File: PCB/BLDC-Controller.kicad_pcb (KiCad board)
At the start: 2 copper layers, 114.3 x 76.5 mm, 95 parts, among them J1 Prog, J2 Receiver, J3 Bat_In, J4 Mot_Con, J5 Mot_Con, J6 Mot_Con, Q1 P75NF75, Q2 P75NF75, Q3 P75NF75, Q4 P75NF75, Q5 P75NF75, Q6 P75NF75, SW1 RST, SW2 Speed+, SW3 Speed-, U1 UCC27282, U2 UCC27282, U3 UCC27282, U4 ATmega328P-P, U5 LM317, U6 LM7805, Y1 16M

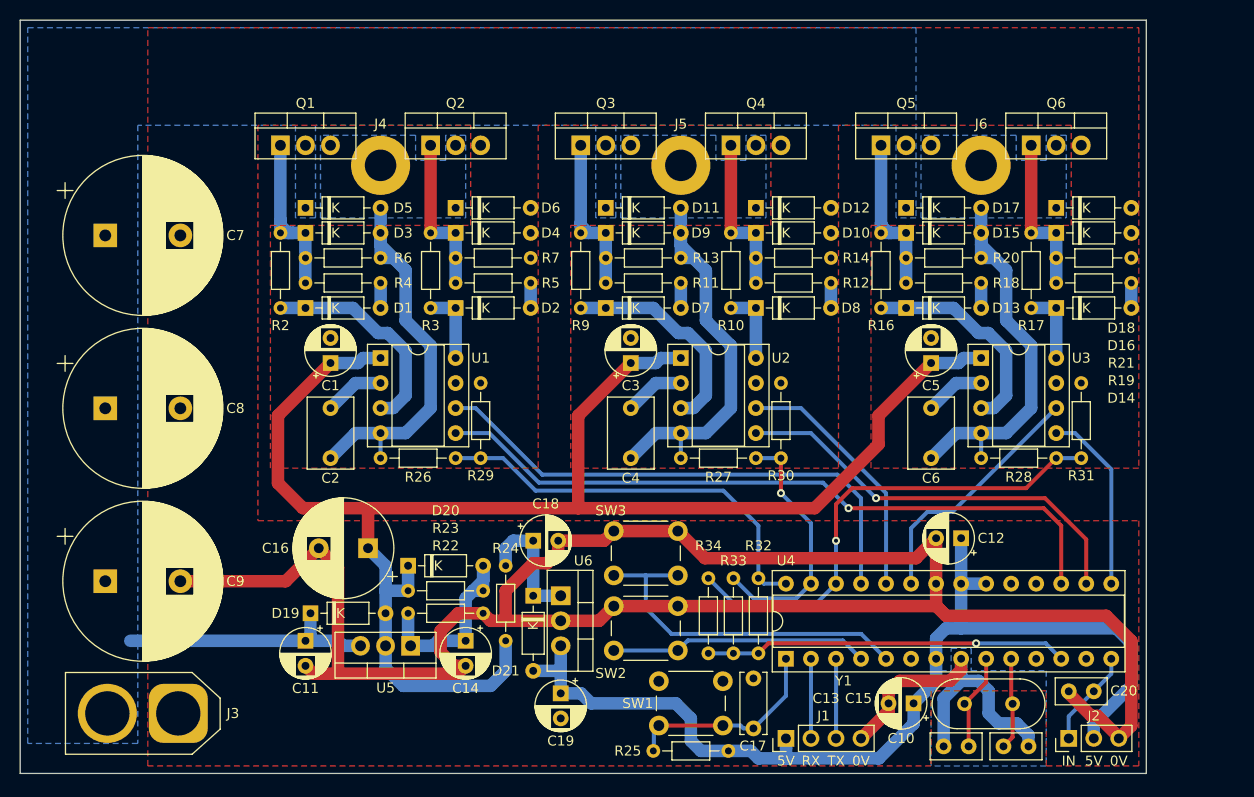
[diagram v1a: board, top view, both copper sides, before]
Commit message: Updated to V1.1. Removed extra parts. Rearranged components. Added on-board LEDs.
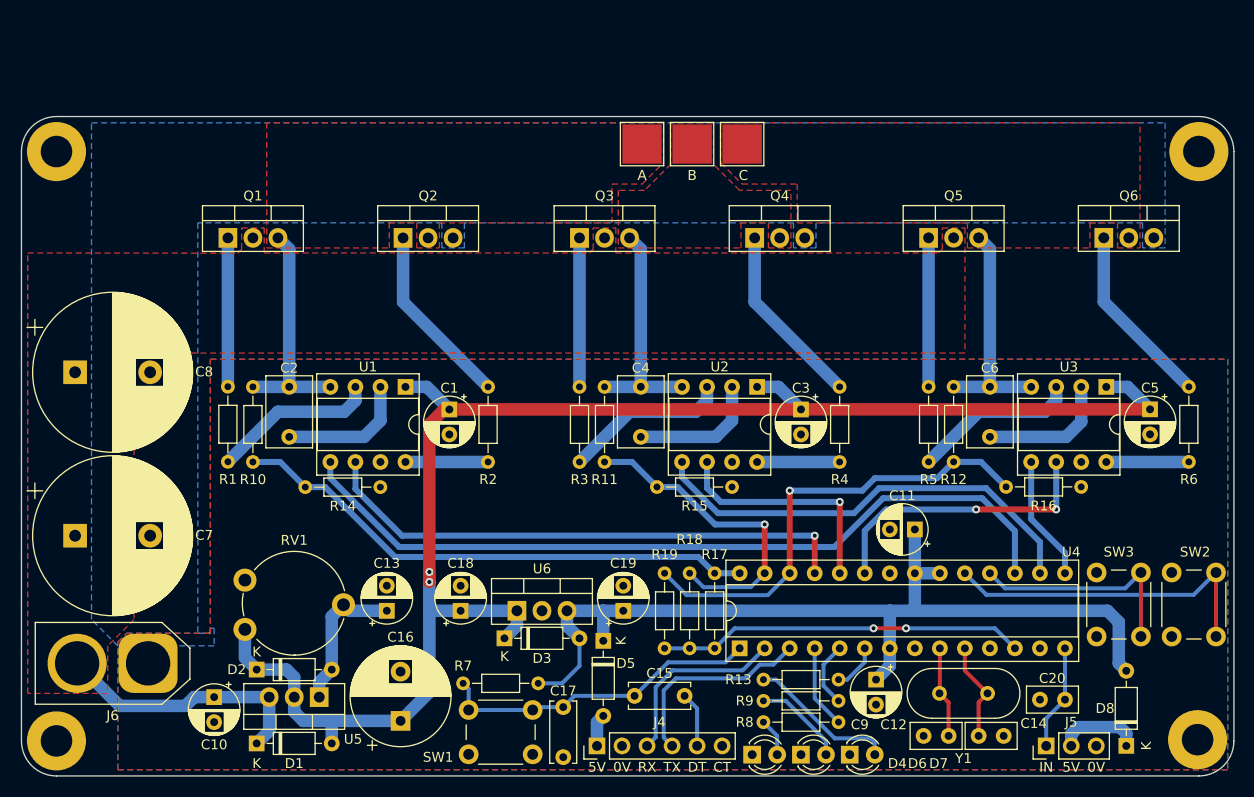
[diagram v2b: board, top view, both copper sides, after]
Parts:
- removed the C9 at (61.0, 75.7)
- removed the D1 at (81.3, 48.0)
- removed D10, D15, D16, D9: 15V, Diode_THT:D_DO-35_SOD27_P7.62mm_Horizontal
- removed D11, D12, D17, D18: 400x, Diode_THT:D_DO-35_SOD27_P7.62mm_Horizontal
- removed D13, D14: 4148, Diode_THT:D_DO-35_SOD27_P7.62mm_Horizontal
- removed the D2 at (96.5, 48.0)
- removed the D3 at (81.3, 40.4)
- removed the J4 at (88.9, 33.5)
- removed the J5 at (119.4, 33.5)
- removed the J6 at (149.9, 33.5)
- removed the R10 at (124.5, 48.0)
- removed the R14 at (127.0, 42.9)
- removed the R16 at (139.7, 48.0)
- removed the R17 at (154.9, 48.0)
- removed the R2 at (78.7, 48.0)
- removed R20, R21: 100k, Resistor_THT:R_Axial_DIN0204_L3.6mm_D1.6mm_P7.62mm_Horizontal
- removed R22: 4k7, Resistor_THT:R_Axial_DIN0204_L3.6mm_D1.6mm_P7.62mm_Horizontal
- removed R23: 560, Resistor_THT:R_Axial_DIN0204_L3.6mm_D1.6mm_P7.62mm_Horizontal
- removed R24: 1, Resistor_THT:R_Axial_DIN0204_L3.6mm_D1.6mm_P7.62mm_Horizontal
- removed the R3 at (94.0, 48.0)
- removed the R6 at (81.3, 42.9)
- removed the R7 at (96.5, 42.9)
- added C15: 100n, Ariamelon-Device:C_Disc_D6.0mm_W2.5mm_P5.08mm, F.Cu at (119.8, 87.4)
- added H1: M3, Ariamelon-HolePad:MountingHole_3.2mm_M3_Pad, F.Cu at (171.8, 91.8)
- added H2: M3, Ariamelon-HolePad:MountingHole_3.2mm_M3_Pad, F.Cu at (56.0, 91.9)
- added H3: M3, Ariamelon-HolePad:MountingHole_3.2mm_M3_Pad, F.Cu at (172.0, 32.1)
- added H4: M3, Ariamelon-HolePad:MountingHole_3.2mm_M3_Pad, F.Cu at (56.0, 32.1)
- added J1: Mot_Con, TestPoint:TestPoint_Pad_4.0x4.0mm, F.Cu at (115.4, 31.4)
- added J2: Mot_Con, TestPoint:TestPoint_Pad_4.0x4.0mm, F.Cu at (120.5, 31.4)
- added J3: Mot_Con, TestPoint:TestPoint_Pad_4.0x4.0mm, F.Cu at (125.6, 31.4)
- added R8: 220, Resistor_THT:R_Axial_DIN0204_L3.6mm_D1.6mm_P7.62mm_Horizontal, F.Cu at (135.4, 90.0)
- added RV1: 10k, Potentiometer_THT:Potentiometer_Piher_PT-10-V10_Vertical, F.Cu at (75.1, 80.6)
- A1: moved to B.Cu
- D4: value 15V -> Red; footprint Diode_THT:D_DO-35_SOD27_P7.62mm_Horizontal -> LED_THT:LED_D3.0mm
- D6: value 400x -> Yellow; footprint Diode_THT:D_DO-35_SOD27_P7.62mm_Horizontal -> LED_THT:LED_D3.0mm
- D7: value 4148 -> Green; footprint Diode_THT:D_DO-35_SOD27_P7.62mm_Horizontal -> LED_THT:LED_D3.0mm
- D8: value 4148 -> 400x
- J4: renamed from J1; footprint Connector_PinHeader_2.54mm:PinHeader_1x04_P2.54mm_Vertical -> Connector_PinHeader_2.54mm:PinHeader_1x06_P2.54mm_Vertical
- R10: renamed from R26; value 47k -> 33k
- R11: renamed from R27; value 47k -> 33k
- R12: renamed from R28; value 47k -> 33k
- R13: value 100k -> 220
- R14: renamed from R29; value 4k7 -> 10k
- R15: renamed from R30; value 4k7 -> 10k
- R16: renamed from R31; value 4k7 -> 10k
- R17: renamed from R32; value 47k -> 33k
- R18: renamed from R33; value 47k -> 33k
- R19: renamed from R34; value 47k -> 33k
- R9: value 22 -> 220
- moved D6 65.6 mm to (131.6, 93.3)
- moved A1 65.0 mm to (145.4, 34.2), turned to 180 degrees
- moved D4 60.9 mm to (126.6, 93.3)
- moved D8 58.2 mm to (164.6, 92.5), turned to 90 degrees
- moved SW2 55.2 mm to (173.7, 74.9), turned to -90 degrees
- moved D5 53.3 mm to (111.5, 81.8), turned to -90 degrees
- moved D7 51.7 mm to (136.5, 93.3)
- moved R13 48.9 mm to (135.4, 85.7), turned to 180 degrees
- moved R9 47.7 mm to (135.4, 87.9), turned to 180 degrees
- moved SW3 47.0 mm to (166.1, 74.9), turned to -90 degrees
- moved C7 30.6 mm to (57.9, 71.1)
- moved SW1 25.9 mm to (97.8, 88.8), turned to 0 degrees
- moved R1 23.9 mm to (73.4, 63.6), turned to 90 degrees
- moved C5 22.7 mm to (167.0, 58.3), turned to -90 degrees
- moved R3 20.9 mm to (109.1, 63.6), turned to 90 degrees
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- renumbered C11 to C10, C12 to C11, C13 to C12, C14 to C13, C15 to C14, C10 to C9, D19 to D1, D20 to D2, D21 to D3, J2 to J5, J3 to J6, R4 to R1, R5 to R2, R11 to R3, R12 to R4, R18 to R5, R19 to R6, R25 to R7
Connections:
- C18 pad 1: Net-(D21-K) -> +12V
- D3 pad 1: Net-(D21-K) -> +12V
- D4 pad 1: Net-(D4-K) -> GND
- D4 pad 2: GND -> Net-(D4-A)
- D5 pad 1: VCC -> +5V
- D5 pad 2: /MCU/Phase_Out_A -> Net-(D5-A)
- D6 pad 1: /MCU/Phase_Out_A -> GND
- D6 pad 2: GND -> Net-(D6-A)
- D7 pad 1: Net-(D7-K) -> GND
- D8 pad 2: Net-(D8-A) -> +5V
- J4 pad 1: +5V -> Net-(D5-A)
- J4 pad 2: RX -> GND
- J4 pad 3: TX -> RX
- J4 pad 4: GND -> TX
- J5 pad 2: +5V -> Net-(D8-K)
- Q2 pad 1: Net-(D4-K) -> Net-(Q2-G)
- Q3 pad 1: Net-(D9-K) -> Net-(Q3-G)
- R1 pad 1: Net-(D1-A) -> Net-(U1-HO)
- R13 pad 1: Net-(D9-K) -> LED_GREEN
- R13 pad 2: /MCU/Phase_Out_B -> Net-(D7-A)
- R2 pad 1: Net-(D2-A) (its old number) -> Net-(U1-LO)
- R2 pad 2: Net-(D4-K) -> Net-(Q2-G)
- R3 pad 1: Net-(D7-A) -> Net-(U2-HO)
- R3 pad 2: Net-(D9-K) -> Net-(Q3-G)
- R4 pad 1: Net-(D8-A) -> Net-(U2-LO)
- R5 pad 1: Net-(D13-A) -> Net-(U3-HO)
- R6 pad 1: Net-(D14-A) -> Net-(U3-LO)
- R9 pad 1: Net-(D7-K) -> LED_YELLOW
- R9 pad 2: Net-(D9-K) -> Net-(D6-A)
- U1 pad 3: Net-(D1-K) -> Net-(U1-HO)
- U1 pad 8: Net-(D2-K) -> Net-(U1-LO)
- U2 pad 3: Net-(D7-K) -> Net-(U2-HO)
- U2 pad 8: Net-(D8-K) -> Net-(U2-LO)
- U3 pad 3: Net-(D13-K) -> Net-(U3-HO)
- U3 pad 8: Net-(D14-K) -> Net-(U3-LO)
- U4 pad 18: unconnected-(U4-PB4-Pad18) -> Speed+
- U4 pad 19: unconnected-(U4-PB5-Pad19) -> Speed-
- U4 pad 4: Speed- -> LED_RED
- U4 pad 5: Speed+ -> LED_YELLOW
- U4 pad 6: unconnected-(U4-PD4-Pad6) -> LED_GREEN
- U6 pad 1: Net-(D21-K) -> +12V
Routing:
- net GND: track 238.8 -> 0.00 mm
- net Net-(D7-K): track 22.1 -> 0.00 mm
- net Net-(D13-K): track 22.1 -> 0.00 mm
- net Net-(D1-K): track 22.1 -> 0.00 mm
- net Net-(Q2-G): track 0.00 -> 18.7 mm
- net Net-(D9-K): track 17.8 -> 0.00 mm
- net /MCU/Phase_Out_A: track 41.1 -> 23.5 mm
- net /MCU/Phase_Out_C: track 41.1 -> 23.5 mm
- net /MCU/Phase_Out_B: track 41.0 -> 23.5 mm
- net Net-(U3-HO): track 0.00 -> 16.9 mm
- net Net-(U2-HO): track 0.00 -> 16.9 mm
- net Net-(U1-HO): track 0.00 -> 16.9 mm
- net Net-(D4-K): track 16.5 -> 0.00 mm
- net Net-(Q3-G): track 0.00 -> 15.1 mm
- net Net-(D21-K): track 13.3 -> 0.00 mm
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- added copper zone on F.Cu, net /MCU/Phase_Out_A
- added copper zone on F.Cu, net /MCU/Phase_Out_B
- added copper zone on F.Cu, net /MCU/Phase_Out_C
- added copper zone on F.Cu, net VCC
- removed copper zone on B.Cu, net /MCU/Phase_Out_A
- removed copper zone on B.Cu, net /MCU/Phase_Out_B
- removed copper zone on B.Cu, net /MCU/Phase_Out_C
- removed copper zone on B.Cu, net VCC
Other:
- board size 114.3 x 76.5 mm -> 123.1 x 66.9 mm
- board text added: "A"
- board text added: "B"
- board text added: "BLDC Motor Controller V1.1"
- board text added: "C"
- board text added: "CT"
- board text added: "DT"
- board text removed: "400x"
- board text removed: "BLDC Motor Controller V1.0"

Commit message: Updated PCB for better grounding.
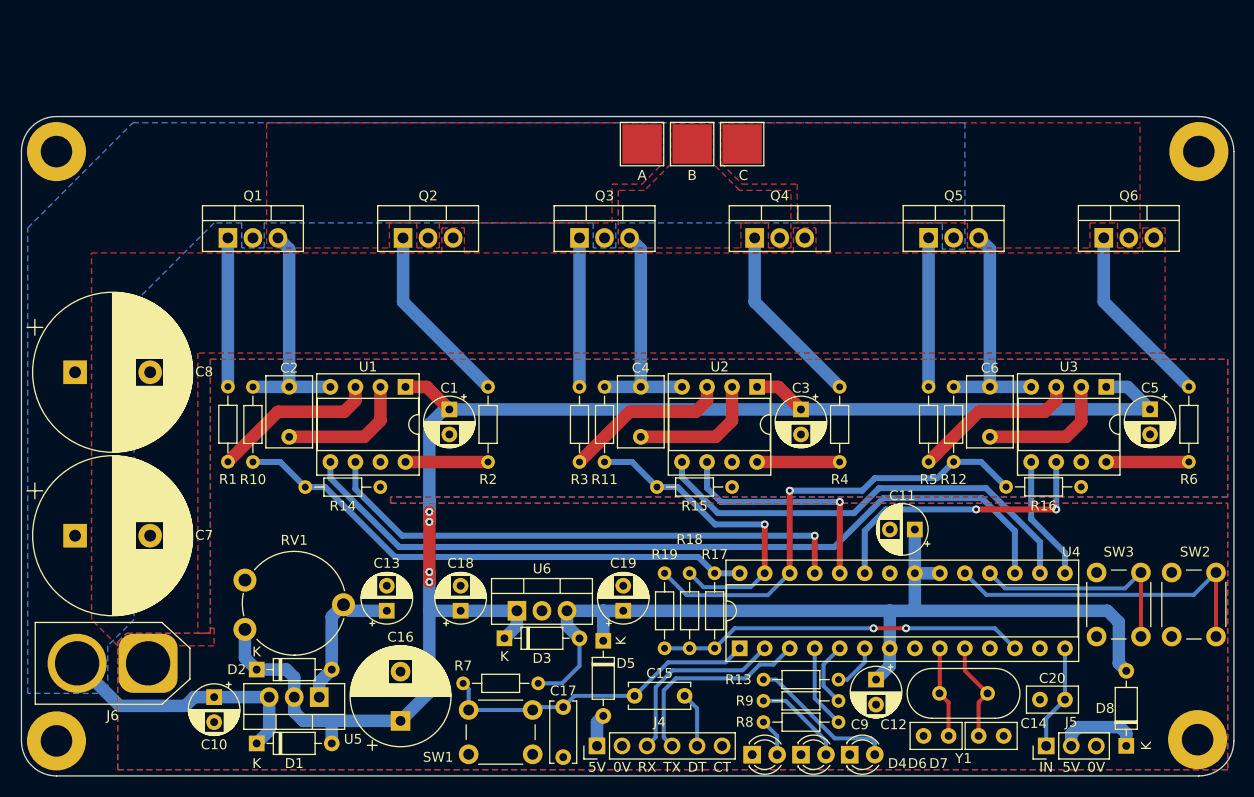
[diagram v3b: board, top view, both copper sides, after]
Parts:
- A1: moved to F.Cu
- moved A1 57.4 mm to (89.5, 47.4), turned to 0 degrees
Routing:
- net +12V: track 160.2 -> 162.1 mm, vias 2 -> 4
- added copper zone on B.Cu, net VCC
- removed copper zone on F.Cu, net VCC

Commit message: Updated firmware.
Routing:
- net /MCU/Phase_Out_B: track 23.5 -> 24.0 mm
- net /MCU/Phase_Out_A: track 23.5 -> 24.0 mm
- net /MCU/Phase_Out_C: track 23.5 -> 24.1 mm
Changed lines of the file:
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@@
   (segment (start 115.951 92.456) (end 116.8282 91.5788) (width 0.4064) (layer "B.Cu") (net 16))
   (segment (start 118.535328 84.7852) (end 125.6538 84.7852) (width 0.4064) (layer "B.Cu") (net 16))
-  (segment (start 79.629 42.037) (end 78.486 40.894) (width 1.27) (layer "B.Cu") (net 17))
+  (segment (start 78.486 43.958) (end 78.486 40.894) (width 1.27) (layer "B.Cu") (net 17))
   (segment (start 83.81 56.017) (end 75.946 56.017) (width 1.27) (layer "B.Cu") (net 17))
-  (segment (start 79.629 56.007) (end 79.629 42.037) (width 1.27) (layer "B.Cu") (net 17))
+  (segment (start 75.946 56.017) (end 75.946 46.498) (width 1.27) (layer "B.Cu") (net 17))
+  (segment (start 75.946 46.498) (end 78.486 43.958) (width 1.27) (layer "B.Cu") (net 17))
+  (segment (start 111.633 46.355) (end 114.173 43.815) (width 1.27) (layer "B.Cu") (net 18))
+  (segment (start 111.633 56.017) (end 111.633 46.355) (width 1.27) (layer "B.Cu") (net 18))
+  (segment (start 114.173 43.815) (end 114.173 40.894) (width 1.27) (layer "B.Cu") (net 18))
   (segment (start 119.497 56.017) (end 111.633 56.017) (width 1.27) (layer "B.Cu") (net 18))
-  (segment (start 115.316 56.007) (end 115.316 42.037) (width 1.27) (layer "B.Cu") (net 18))
-  (segment (start 115.316 42.037) (end 114.173 40.894) (width 1.27) (layer "B.Cu") (net 18))
+  (segment (start 149.606 43.942) (end 149.606 40.884) (width 1.27) (layer "B.Cu") (net 19))
   (segment (start 147.076 56.017) (end 147.066 56.007) (width 1.27) (layer "B.Cu") (net 19))
   (segment (start 154.94 56.017) (end 147.076 56.017) (width 1.27) (layer "B.Cu") (net 19))
-  (segment (start 150.749 56.007) (end 150.749 42.027) (width 1.27) (layer "B.Cu") (net 19))
-  (segment (start 150.749 42.027) (end 149.606 40.884) (width 1.27) (layer "B.Cu") (net 19))
+  (segment (start 147.066 46.482) (end 149.606 43.942) (width 1.27) (layer "B.Cu") (net 19))
+  (segment (start 147.066 56.007) (end 147.066 46.482) (width 1.27) (layer "B.Cu") (net 19))
   (segment (start 91.186 40.894) (end 91.186 47.391) (width 1.27) (layer "B.Cu") (net 20))
   (segment (start 91.186 47.391) (end 99.812 56.017) (width 1.27) (layer "B.Cu") (net 20))

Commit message: Fixed issues with code. Updated schematic.
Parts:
- added C14: 100n, Ariamelon-Device:C_Disc_D6.0mm_W2.5mm_P5.08mm, F.Cu at (142.7, 85.7)
- added C15: 100n, Ariamelon-Device:C_Disc_D6.0mm_W2.5mm_P5.08mm, F.Cu at (145.7, 71.8)
- added C2: 100n, Ariamelon-Device:C_Disc_D6.0mm_W2.5mm_P5.08mm, F.Cu at (94.7, 56.0)
- added C5: 100n, Ariamelon-Device:C_Disc_D6.0mm_W2.5mm_P5.08mm, F.Cu at (130.3, 56.0)
- added C8: 100n, Ariamelon-Device:C_Disc_D6.0mm_W2.5mm_P5.08mm, F.Cu at (165.9, 56.0)
- J1: value Mot_Con -> Mot_Con_A
- J2: value Mot_Con -> Mot_Con_B
- J3: value Mot_Con -> Mot_Con_C
- moved C18 5.97 mm to (161.8, 87.8), turned to 180 degrees
- moved C7 5.60 mm to (172.6, 58.3)
- moved C1 5.60 mm to (101.5, 58.3)
- moved C4 5.60 mm to (137.2, 58.3)
- moved C13 5.25 mm to (148.4, 70.5), turned to 0 degrees
- moved C12 4.68 mm to (142.7, 88.8)
- moved C10 3.43 mm to (147.4, 91.4)
- moved C11 3.43 mm to (155.6, 91.4)
- moved Y1 3.43 mm to (149.1, 87.1)
- moved J5 2.79 mm to (159.3, 92.5)
- moved D5 2.79 mm to (167.4, 92.5)
- moved R6 2.40 mm to (168.5, 63.6)
- moved R2 2.40 mm to (97.4, 63.6)
- moved R4 2.40 mm to (133.1, 63.6)
- moved C24 1.31 mm to (88.4, 78.1), turned to 0 degrees
- renumbered C12 to C10, C14 to C11, C9 to C12, C11 to C13, C15 to C16, C20 to C18, C18 to C19, C7 to C20, C8 to C21, C19 to C22, C10 to C23, C13 to C24, C16 to C25, C2 to C3, C3 to C4, C4 to C6, C5 to C7, C6 to C9, D4 to D1, D6 to D2, D7 to D3, D5 to D4, D8 to D5, D3 to D6, D1 to D7, D2 to D8, R12 to R10, R14 to R11, R15 to R12, R16 to R13, R17 to R14, R18 to R15, R19 to R16, R8 to R17, R9 to R18, R13 to R19, R10 to R8, R11 to R9, U6 to U5, U5 to U6
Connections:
- net +12V renamed Vdrive
- net /MCU/HI_A renamed HI_A
- net /MCU/HI_B renamed HI_B
- net /MCU/HI_C renamed HI_C
- net /MCU/LI_A renamed LI_A
- net /MCU/LI_B renamed LI_B
- net /MCU/LI_C renamed LI_C
- net /MCU/Phase_Out_A renamed Phase_Out_A
- net /MCU/Phase_Out_B renamed Phase_Out_B
- net /MCU/Phase_Out_C renamed Phase_Out_C
- SW2 pad 1: Speed- -> Speed+
- SW3 pad 1: Speed+ -> Speed-
- U4 pad 18: Speed+ -> Speed-
- U4 pad 19: Speed- -> Speed+
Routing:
- net Vdrive: track 162.1 -> 219.5 mm, vias 4 -> 0
- net Speed-: track 33.8 -> 23.1 mm
- net Speed+: track 23.1 -> 33.8 mm
- net +5V: track 94.2 -> 103.1 mm
- net GND: track 0.00 -> 7.53 mm
- net Net-(U3-LO): track 8.41 -> 6.00 mm
- net Net-(U2-LO): track 8.38 -> 5.98 mm
- net Net-(U1-LO): track 8.38 -> 5.98 mm
- net XTAL2: track 10.2 -> 12.3 mm
- net Net-(D5-K): track 8.61 -> 7.06 mm
- net XTAL1: track 9.29 -> 10.7 mm
- net Net-(D8-A): track 15.0 -> 13.7 mm
- net Net-(Q6-G): track 18.7 -> 17.7 mm
- net Net-(Q4-G): track 18.7 -> 17.7 mm
- net Net-(Q2-G): track 18.7 -> 17.7 mm
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
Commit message: Final update before project completion.
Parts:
- J1: value Mot_Con_A -> Phase_A
- J2: value Mot_Con_B -> Phase_B
- J3: value Mot_Con_C -> Phase_C
- R11: renamed from R8; value 33k -> 47k
- R12: renamed from R9; value 33k -> 47k
- R13: renamed from R10; value 33k -> 47k
- R17: renamed from R14; value 33k -> 47k
- R18: renamed from R15; value 33k -> 47k
- R19: renamed from R16; value 33k -> 47k
- renumbered C20 to C19, C21 to C20, C23 to C21, C24 to C22, C25 to C23, C19 to C24, C22 to C25, D7 to D6, D8 to D7, D6 to D8, R19 to R10, R11 to R14, R12 to R15, R13 to R16, R17 to R8, R18 to R9, U6 to U5, U5 to U6
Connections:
- net LI_A renamed LO_A
- net LI_B renamed LO_B
- net LI_C renamed LO_C
